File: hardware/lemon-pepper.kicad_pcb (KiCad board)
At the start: 4 copper layers, 35 x 35 mm, 78 parts, among them J101 INPUT, J201 USB_C_Receptacle_USB2.0, J301 TagConnect, M101 MOT, Q501 MMBT5551, U201 SRV05-4, U301 STM32G431, U302 SN65HVD230, U401 MT6835, U501 MAX15062CATA+T, U601 L6226QTR, U701 ACS711KEXLT-15AB-T, U702 ACS711KEXLT-15AB-T, U703 ACS711KEXLT-15AB-T, Y301 12MHz

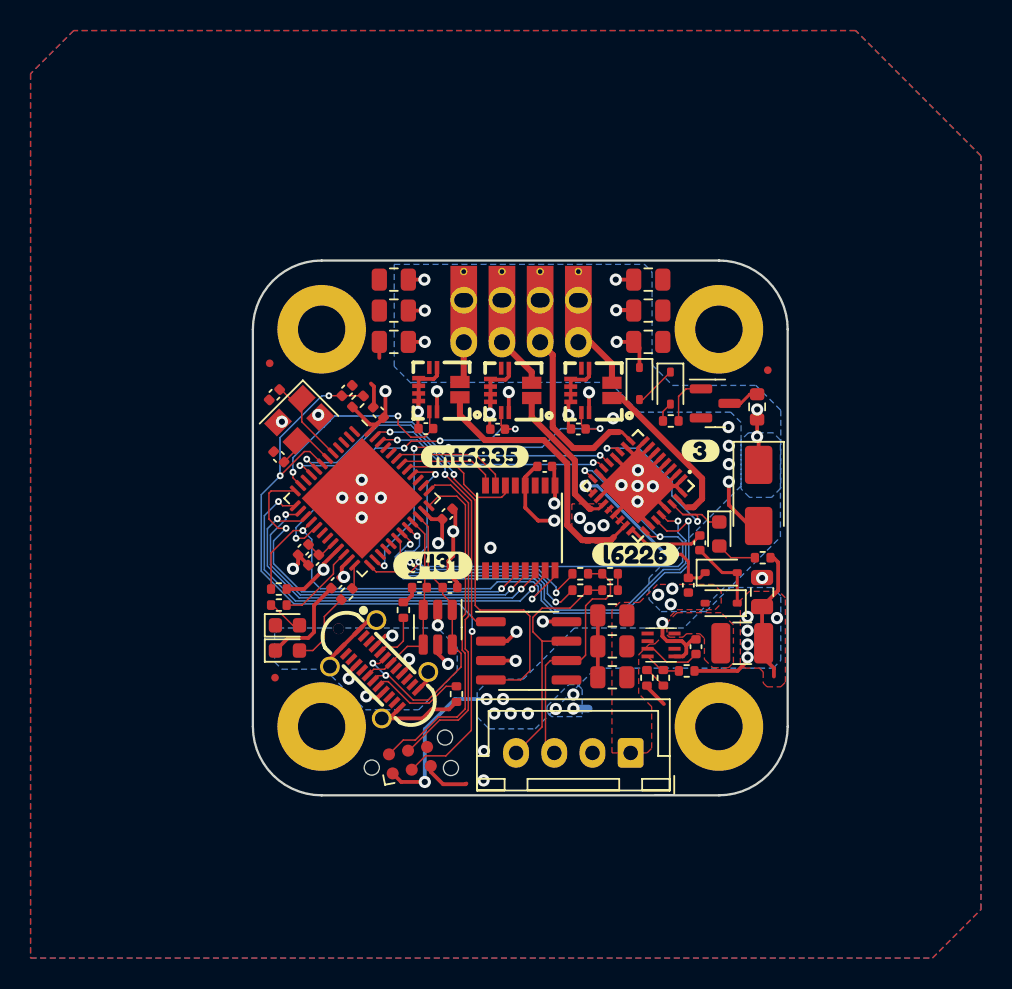
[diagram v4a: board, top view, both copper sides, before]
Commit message: redraw USB C connector with proper mounting holes
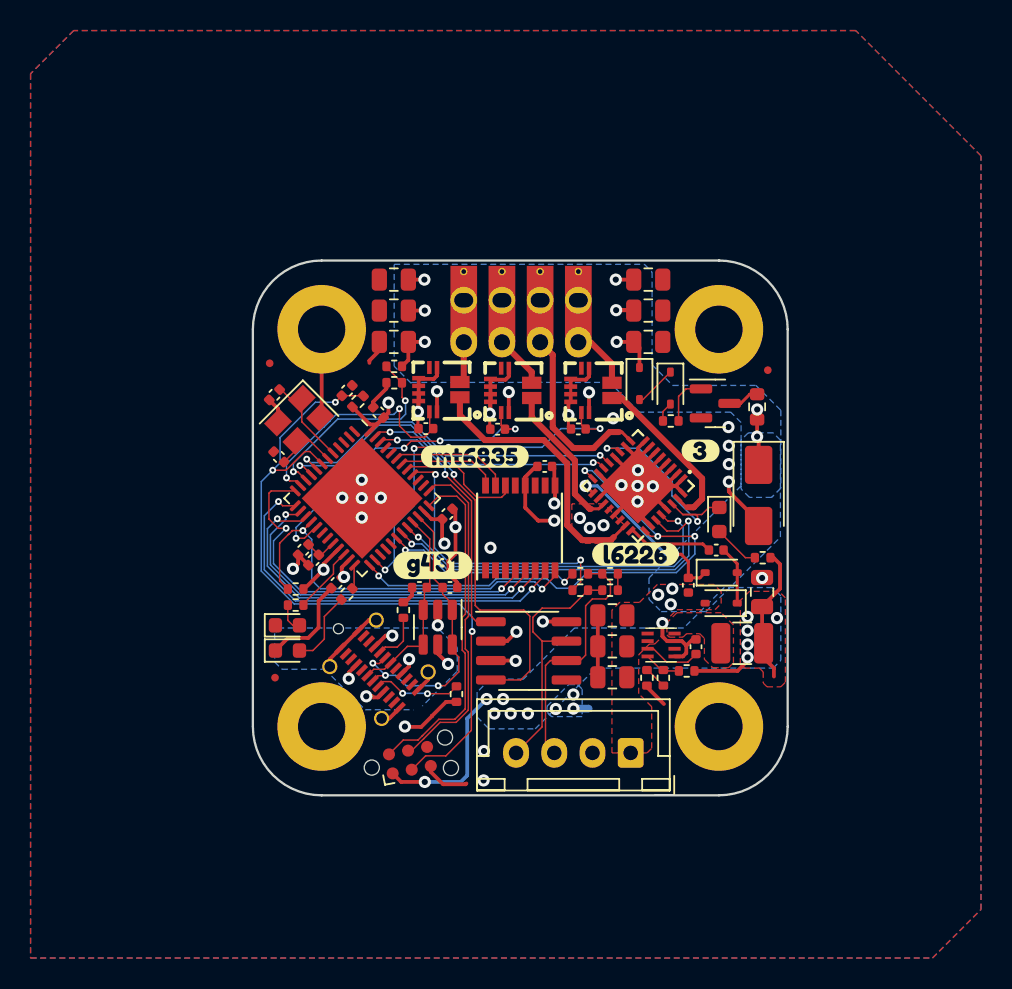
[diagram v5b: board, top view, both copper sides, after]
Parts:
- added R303: 51k, Resistor_SMD:R_0402_1005Metric, F.Cu at (138.1, 76.4)
- added R304: 3k, Resistor_SMD:R_0402_1005Metric, F.Cu at (138.1, 77.5)
- J201: footprint easyeda2kicad:USB-C-SMD_GT-USB-7052_1 -> mechanical:usb_c
- moved C601 1.18 mm to (159.1, 88.4), turned to 180 degrees
- moved R301 1.10 mm to (131.6, 92.0)
- moved R401 1.10 mm to (131.6, 91.0)
- moved D601 0.95 mm to (159.3, 86.4)
- moved J201 0.15 mm to (137.0, 96.1)
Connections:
- U301 pad 10: unconnected-(U301-PA2-Pad10) -> /mcu/ADC1_IN12
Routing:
- net /mcu/ADC1_IN12: track 0.00 -> 13.9 mm, vias 0 -> 2
- net /half bridges/IN2A: track 30.0 -> 23.1 mm
- net GND: track 97.1 -> 103.9 mm, vias 28 -> 27
- net /half bridges/IN1A: track 31.0 -> 25.2 mm
- net /mcu/STEP: track 22.0 -> 18.7 mm
- net /half bridges/ENA: track 32.8 -> 35.2 mm, vias 3 -> 4
- net Vmot: track 13.3 -> 15.0 mm
- net /encoder/CS: track 28.2 -> 26.6 mm
- net +3V3: track 64.5 -> 63.2 mm
- net /current sense/U_SENSE: track 14.7 -> 16.0 mm
- net /mcu/DIR: track 14.4 -> 13.1 mm
- net Net-(D602-K): track 5.06 -> 3.85 mm
- net Net-(U301-PB10): track 5.46 -> 4.41 mm
- net /mcu/USBD_P: track 20.7 -> 19.8 mm, vias 2 -> 3
- net Net-(U601-VCP): track 5.10 -> 5.63 mm
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
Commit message: work on current sense
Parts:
- R304: value 3k -> 3k3
- moved JP101 6.44 mm to (145.8, 91.8)
- moved R105 6.41 mm to (143.8, 91.8)
- moved R103 4.81 mm to (147.7, 91.8), turned to 180 degrees
- moved R104 1.87 mm to (149.6, 91.8), turned to 0 degrees
- moved C201 0.62 mm to (139.1, 90.9)
- moved C202 0.50 mm to (141.2, 90.9)
- moved kibuzzard-6547C3FC 0.40 mm to (157.7, 81.9)
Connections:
- U301 pad 39: unconnected-(U301-PC10-Pad39) -> /mcu/DIR
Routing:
- net /mcu/DIR: track 13.1 -> 20.6 mm, vias 2 -> 3
- net /mcu/CANL: track 16.5 -> 14.4 mm
- net /mcu/STEP: track 18.7 -> 16.8 mm
- net /mcu/CANH: track 16.7 -> 15.4 mm
- net /encoder/Z: track 8.36 -> 8.99 mm
- net /half bridges/ENA: track 35.2 -> 35.8 mm
- net /encoder/CS: track 26.6 -> 27.2 mm
- net /mcu/CAN_RX: track 25.9 -> 26.5 mm

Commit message: update pcb layout
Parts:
- added C109: 10u, Capacitor_SMD:C_0805_2012Metric, F.Cu at (152.3, 90.7)
- added J302: USER CONN., mechanical:PinHeader_1x05_P1.27mm_SMD, F.Cu at (127.0, 90.0)
- moved kibuzzard-65305A5A 1.08 mm to (152.8, 88.8)
- moved D301 0.90 mm to (131.5, 94.2)
- moved FID102 0.90 mm to (129.7, 97.5)
- moved R301 0.88 mm to (132.0, 92.8)
- moved D302 0.88 mm to (131.5, 95.8)
- moved R401 0.84 mm to (132.0, 91.7)
- turned H101 to 0 degrees
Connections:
- U301 pad 27: unconnected-(U301-PB14-Pad27) -> /mcu/USER_3
- U301 pad 28: unconnected-(U301-PB15-Pad28) -> /mcu/USER_2
- U301 pad 29: unconnected-(U301-PC6-Pad29) -> /mcu/USER_1
- U301 pad 44: unconnected-(U301-PB6-Pad44) -> /mcu/TIM4_CH1
- U301 pad 45: unconnected-(U301-PB7-Pad45) -> /mcu/TIM4_CH2
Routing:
- net /mcu/TIM4_CH2: track 0.00 -> 16.0 mm, vias 0 -> 2
- net /mcu/TIM4_CH1: track 0.00 -> 14.8 mm, vias 0 -> 2
- net /mcu/USER_1: track 0.00 -> 13.5 mm, vias 0 -> 2
- net /mcu/USER_2: track 0.00 -> 13.0 mm, vias 0 -> 2
- net /mcu/USER_3: track 0.00 -> 12.8 mm, vias 0 -> 2
- net +3V3: track 63.2 -> 64.9 mm
- net Net-(U301-PB11): track 1.59 -> 3.16 mm
- net GND: track 103.6 -> 102.3 mm
- net /encoder/CAL_EN: track 25.3 -> 24.2 mm
- net /current sense/U_SENSE: track 16.0 -> 17.1 mm
- net /mcu/CAN_TX: track 17.4 -> 18.4 mm
- net /encoder/COPI: track 25.2 -> 26.1 mm
- net /mcu/CAN_RX: track 26.5 -> 27.2 mm
- net /encoder/SCK: track 26.3 -> 27.0 mm
- net /encoder/CIPO: track 23.6 -> 24.3 mm
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
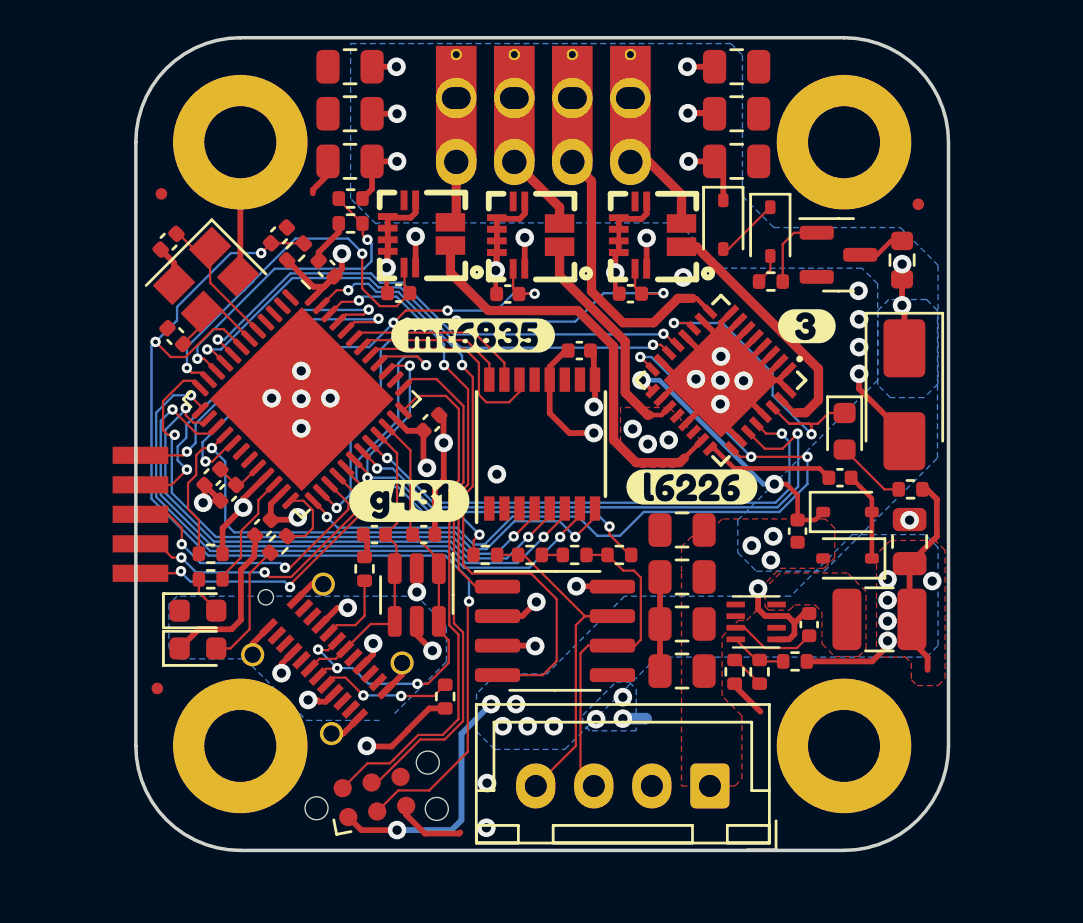
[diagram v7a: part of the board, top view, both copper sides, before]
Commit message: add user button
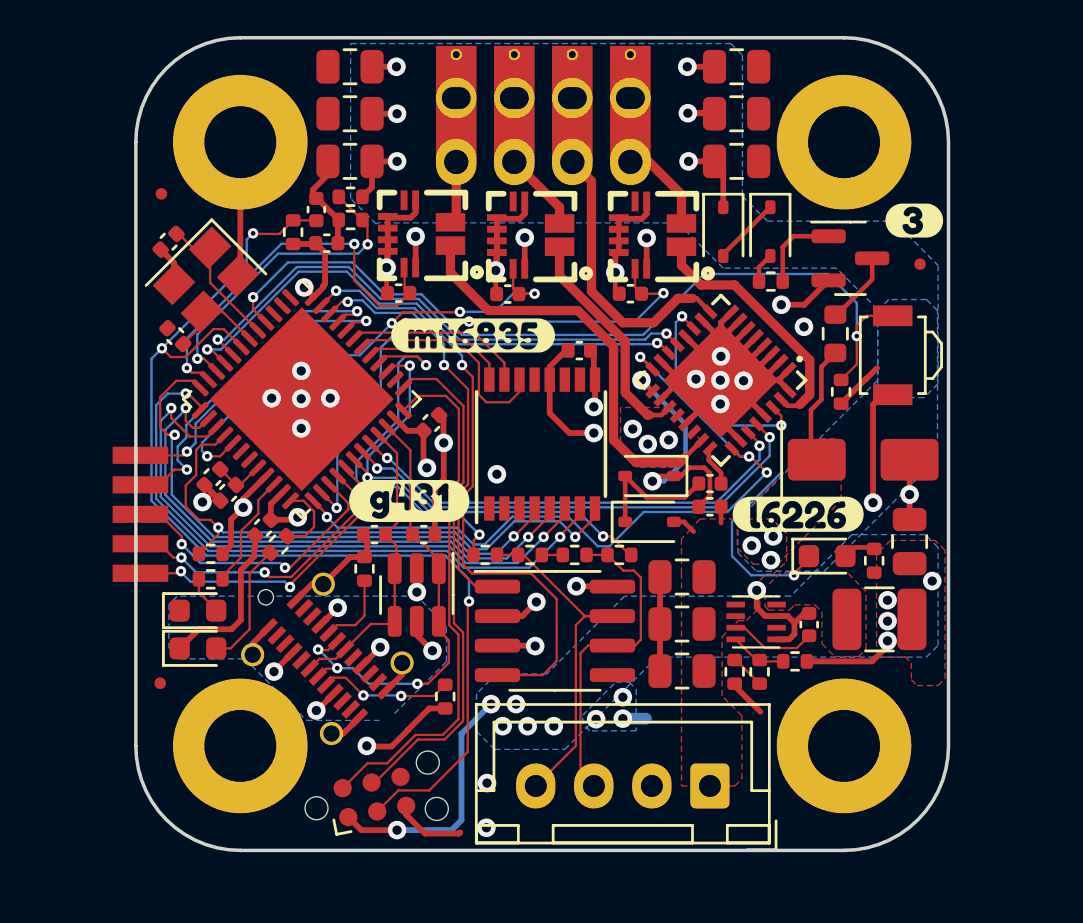
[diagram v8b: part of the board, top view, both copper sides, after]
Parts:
- removed C109: 10u, Capacitor_SMD:C_0805_2012Metric
- added R305: 10k, Resistor_SMD:R_0402_1005Metric, F.Cu at (159.2, 84.7)
- added SW301: USER, Button_Switch_SMD:SW_SPST_B3U-3000P, F.Cu at (161.4, 83.2)
- moved D602 8.67 mm to (150.9, 90.3), turned to 0 degrees
- moved D603 8.66 mm to (150.9, 88.3), turned to 180 degrees
- moved kibuzzard-6547C3FC 6.49 mm to (162.3, 77.3)
- moved C601 5.61 mm to (153.5, 88.7), turned to 0 degrees
- moved D601 5.43 mm to (158.6, 91.8), turned to 0 degrees
- moved kibuzzard-65305A5A 4.72 mm to (157.3, 90.0)
- moved R504 4.28 mm to (158.9, 82.2)
- moved C602 3.92 mm to (153.5, 89.7), turned to 0 degrees
- moved R601 3.45 mm to (160.6, 92.0), turned to -90 degrees
- moved D101 3.32 mm to (160.1, 87.7), turned to 0 degrees
- moved FID103 2.58 mm to (162.6, 79.2)
- moved C308 1.96 mm to (136.6, 76.9), turned to 90 degrees
- moved C303 1.09 mm to (137.0, 78.3), turned to 0 degrees
- moved R306 0.86 mm to (135.6, 77.8), turned to 90 degrees
- moved Q501 0.53 mm to (159.6, 79.0)
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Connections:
- U301 pad 31: /half bridges/IN1A -> /half bridges/IN2A
- U301 pad 32: /half bridges/IN2A -> /half bridges/IN1A
- U301 pad 4: unconnected-(U301-PC15-Pad4) -> /mcu/USER_BTN
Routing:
- net /mcu/USER_BTN: track 0.00 -> 36.6 mm, vias 0 -> 2
- net GND: track 102.3 -> 110.0 mm, vias 27 -> 24
- net Net-(D601-K): track 14.3 -> 20.6 mm, vias 2 -> 3
- net /half bridges/IN1A: track 25.2 -> 20.0 mm
- net /half bridges/ENA: track 35.8 -> 31.9 mm
- net Net-(U601-VCP): track 5.63 -> 1.75 mm
- net Vmot: track 15.0 -> 18.5 mm, vias 14 -> 12
- net /encoder/CS: track 27.5 -> 25.5 mm
- net /half bridges/IN2A: track 23.1 -> 21.1 mm
- net Net-(D602-K): track 3.85 -> 5.78 mm
- net Net-(D601-A): track 3.04 -> 1.42 mm
- net Net-(Q501-C): track 2.05 -> 3.63 mm
- net /mcu/TIM4_CH1: track 14.8 -> 13.6 mm
- net /mcu/TIM4_CH2: track 16.0 -> 14.9 mm
- net /usb/USB_5V: track 6.63 -> 6.01 mm
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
